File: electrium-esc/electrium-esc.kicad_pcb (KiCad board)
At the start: 2 copper layers, 87.1 x 57.9 mm, 189 parts, among them J1 Debug Connector, J2 USB_MICRO, J3 Conn_01x04_Male, J4 SERVO, J5 Conn_01x04_Male, Q1 IRF3205, Q10 IRF3205, Q11 IRF3205, Q12 IRF3205, Q2 IRF3205, Q3 IRF3205, Q4 IRF3205, Q5 IRF3205, Q6 IRF3205, Q7 IRF3205, Q8 IRF3205, Q9 IRF3205, SW1 SW_SPDT, U1 STM32F407ZGT6, U2 DRV8301DCAR, U3 DRV8301DCAR, U4 SN65HVD232, U5 NRF24L01_Breakout, Y1 25MHz

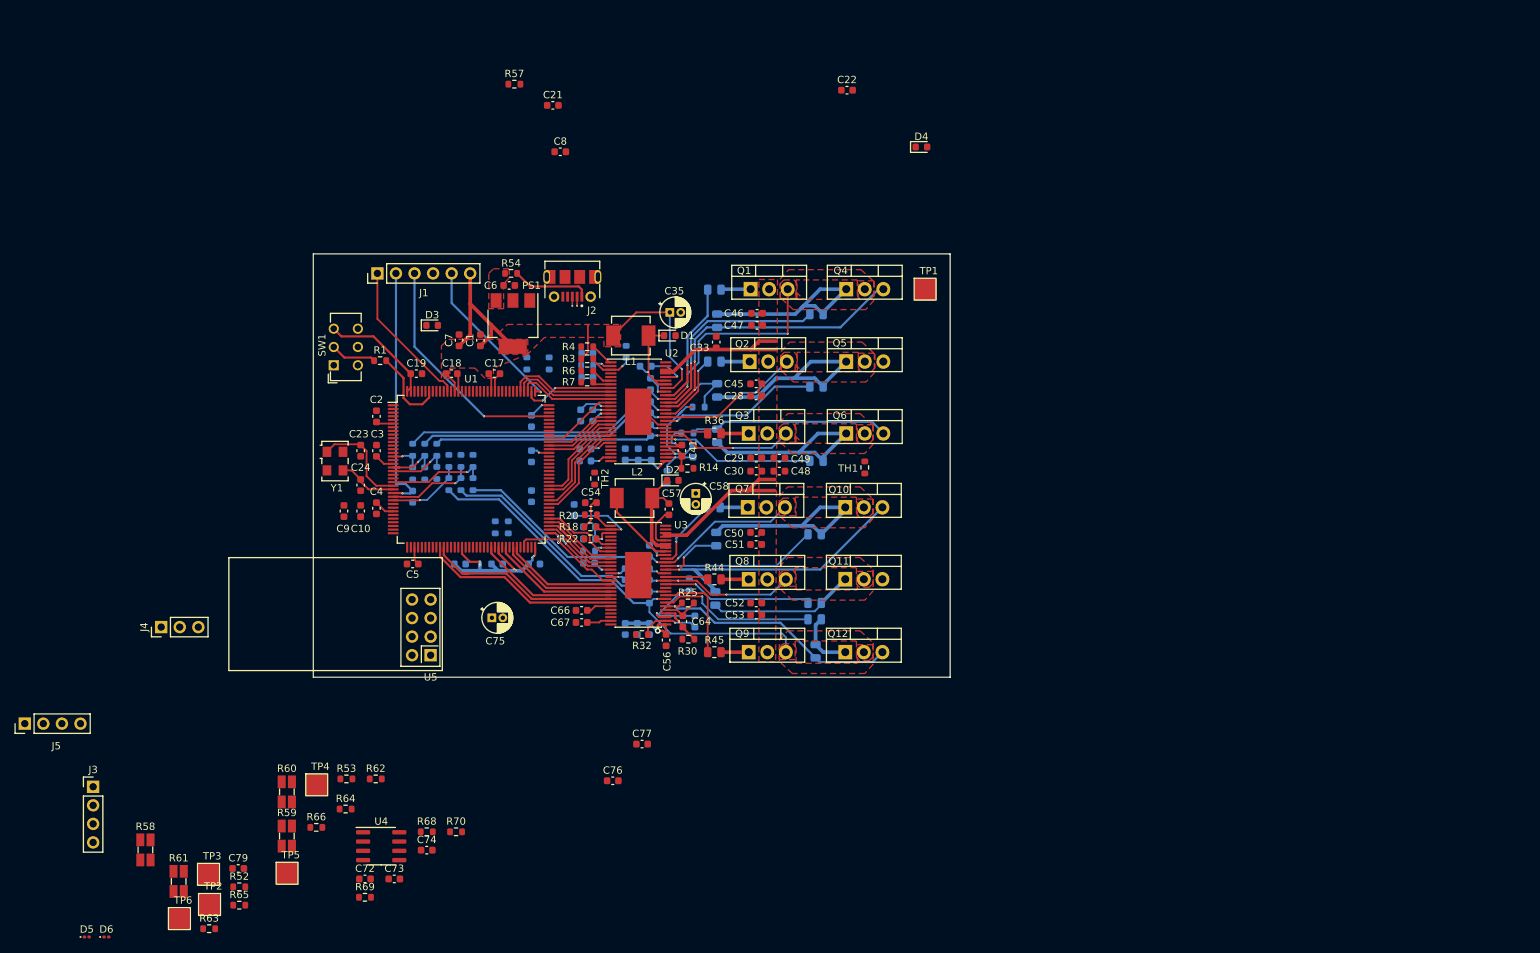
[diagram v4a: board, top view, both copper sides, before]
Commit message: Add power connections
I realize Vias are unrealistic, need to redo.
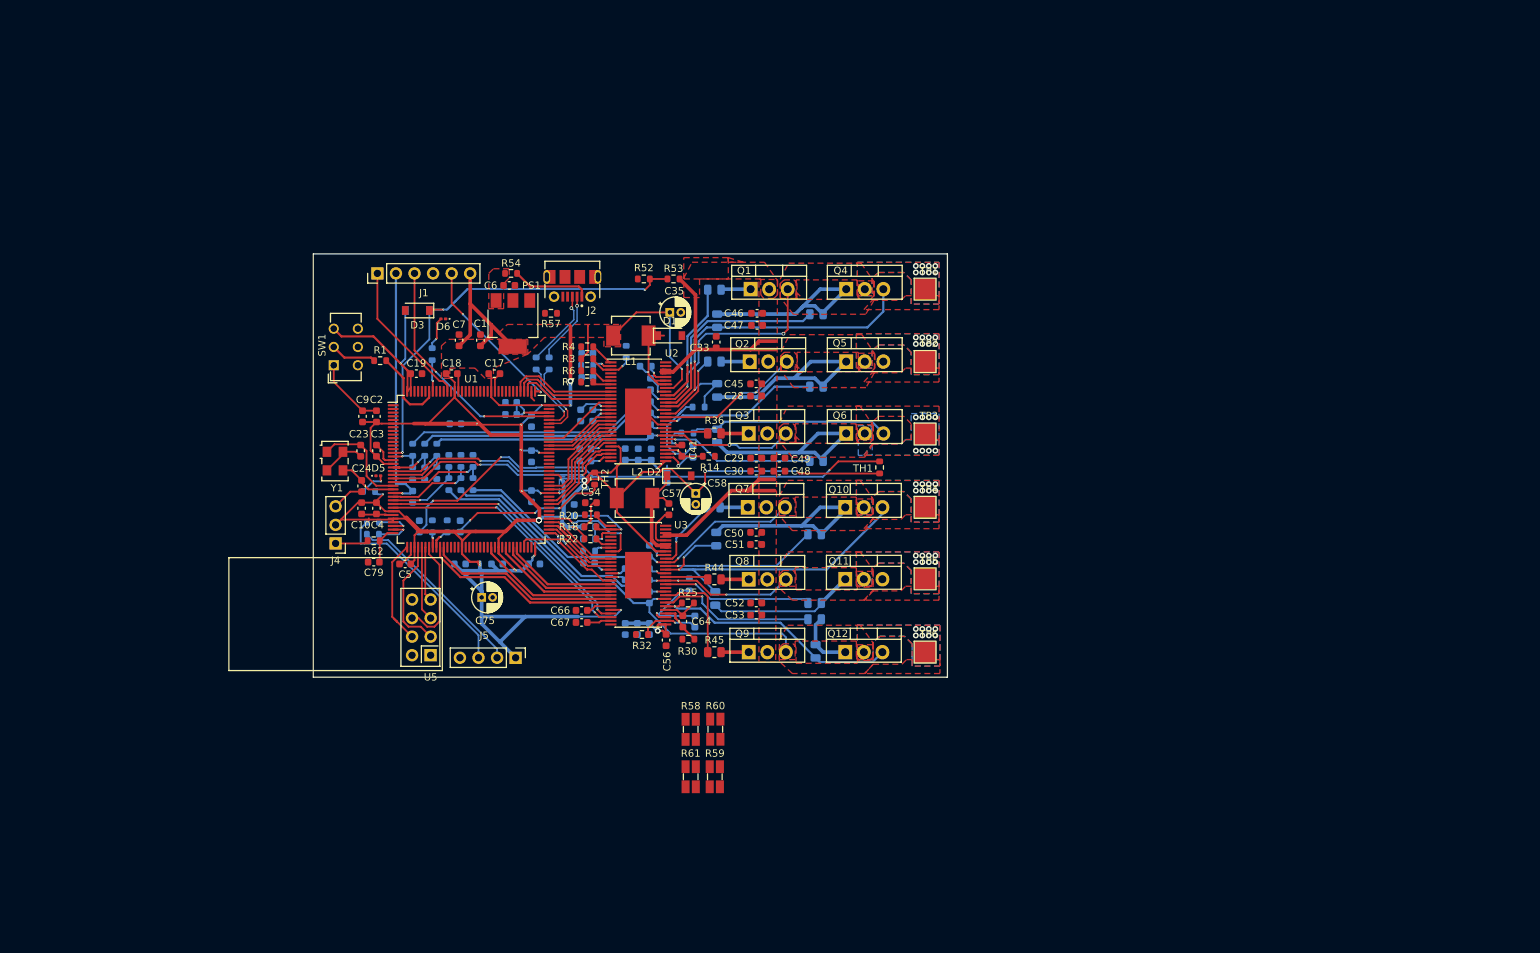
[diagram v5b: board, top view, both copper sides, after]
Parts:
- removed C72, C73, C74: 100n, Capacitor_SMD:C_0603_1608Metric
- removed J3: Conn_01x04_Male, Connector_PinHeader_2.54mm:PinHeader_1x04_P2.54mm_Vertical
- removed R68, R69: 10, Resistor_SMD:R_0603_1608Metric
- removed R70: IN, Resistor_SMD:R_0603_1608Metric
- removed U4: SN65HVD232, Package_SO:SOIC-8_3.9x4.9mm_P1.27mm
- C21, C22, C76, C77, C8, R63, R64, R65, R66: moved to B.Cu
- D1, D2, D3: footprint Diode_SMD:D_0603_1608Metric -> Diode_SMD:D_SOD-123
- D4: footprint Diode_SMD:D_0603_1608Metric -> Diode_SMD:D_SOD-123; moved to B.Cu
- moved TP2 122.9 mm to (186.1, 61.5)
- moved TP3 115.1 mm to (186.1, 71.4)
- moved TP6 108.3 mm to (186.1, 101.2)
- moved R52 99.9 mm to (147.6, 50.2)
- moved D6 96.3 mm to (120.1, 55.6), turned to 180 degrees
- moved TP5 96.1 mm to (186.1, 91.2)
- moved TP4 91.5 mm to (186.1, 81.4)
- moved R53 81.7 mm to (151.6, 50.2)
- moved R58 76.4 mm to (154.0, 111.8)
- moved D5 74.6 mm to (111.3, 77.1)
- moved D4 72.5 mm to (116.6, 54.5)
- moved R61 71.5 mm to (154.0, 118.3)
- moved J5 67.8 mm to (130.0, 102.0), turned to -90 degrees
- moved R66 66.6 mm to (118.6, 60.5), turned to -90 degrees
- moved C22 63.9 mm to (129.4, 68.7), turned to 180 degrees
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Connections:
- J4 pad 2: +5V -> +3.3V
- U1 pad 114: /CAN_RX -> /MCU (STM32F407ZGT6)/CAN_RX
- U1 pad 115: /CAN_TX -> /MCU (STM32F407ZGT6)/CAN_TX
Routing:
- net +3.3V: track 123.0 -> 443.1 mm, vias 10 -> 31
- net /MCU (STM32F407ZGT6)/TEMP_A: track 0.00 -> 74.5 mm, vias 0 -> 4
- net /AN_IN: track 0.00 -> 63.2 mm, vias 0 -> 4
- net /MCU (STM32F407ZGT6)/BR_SO2_B: track 0.00 -> 36.6 mm, vias 0 -> 2
- net /MCU (STM32F407ZGT6)/BR_SO1_B: track 0.00 -> 36.5 mm, vias 0 -> 2
- net /MCU (STM32F407ZGT6)/BR_SO2_A: track 0.00 -> 34.8 mm, vias 0 -> 2
- net /MCU (STM32F407ZGT6)/BR_SO1_A: track 0.00 -> 33.1 mm, vias 0 -> 2
- net GND: track 9.96 -> 41.6 mm
- net Net-(J5-Pad3): track 0.00 -> 28.2 mm
- net /MCU (STM32F407ZGT6)/TEMP_B: track 0.00 -> 26.3 mm, vias 0 -> 4
- net Net-(J5-Pad2): track 0.00 -> 25.5 mm
- net /MCU (STM32F407ZGT6)/NRF_CE: track 0.00 -> 15.8 mm
- net /MCU (STM32F407ZGT6)/NRF_MOSI: track 0.00 -> 15.3 mm
- net /MCU (STM32F407ZGT6)/NRF_CSN: track 0.00 -> 15.0 mm
- net V_SUPPLY: track 59.0 -> 70.9 mm
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- added copper zone on B.Cu, net +3.3V
- added copper zone on B.Cu, net /Motor Driver A (DRV8301)/H1_VS
- added copper zone on B.Cu, net /Motor Driver A (DRV8301)/H2_VS
- added copper zone on B.Cu, net /Motor Driver A (DRV8301)/H3_VS
- added copper zone on B.Cu, net /Motor Driver B (DRV8301)/H1_VS
- added copper zone on B.Cu, net /Motor Driver B (DRV8301)/H2_VS
- added copper zone on B.Cu, net /Motor Driver B (DRV8301)/H3_VS
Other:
- board size 87.1 x 57.9 mm -> 86.7 x 57.9 mm

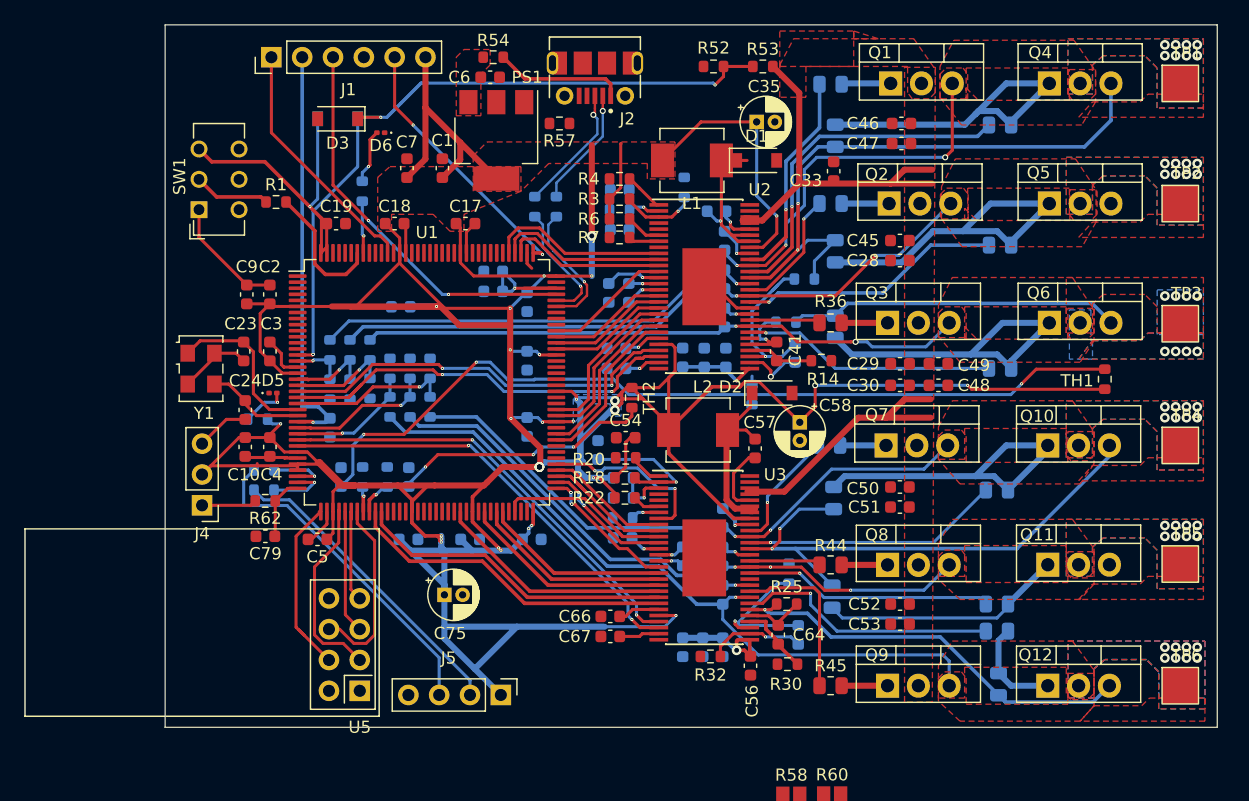
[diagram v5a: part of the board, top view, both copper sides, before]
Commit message: Fix most ERC errors, just some connections now!
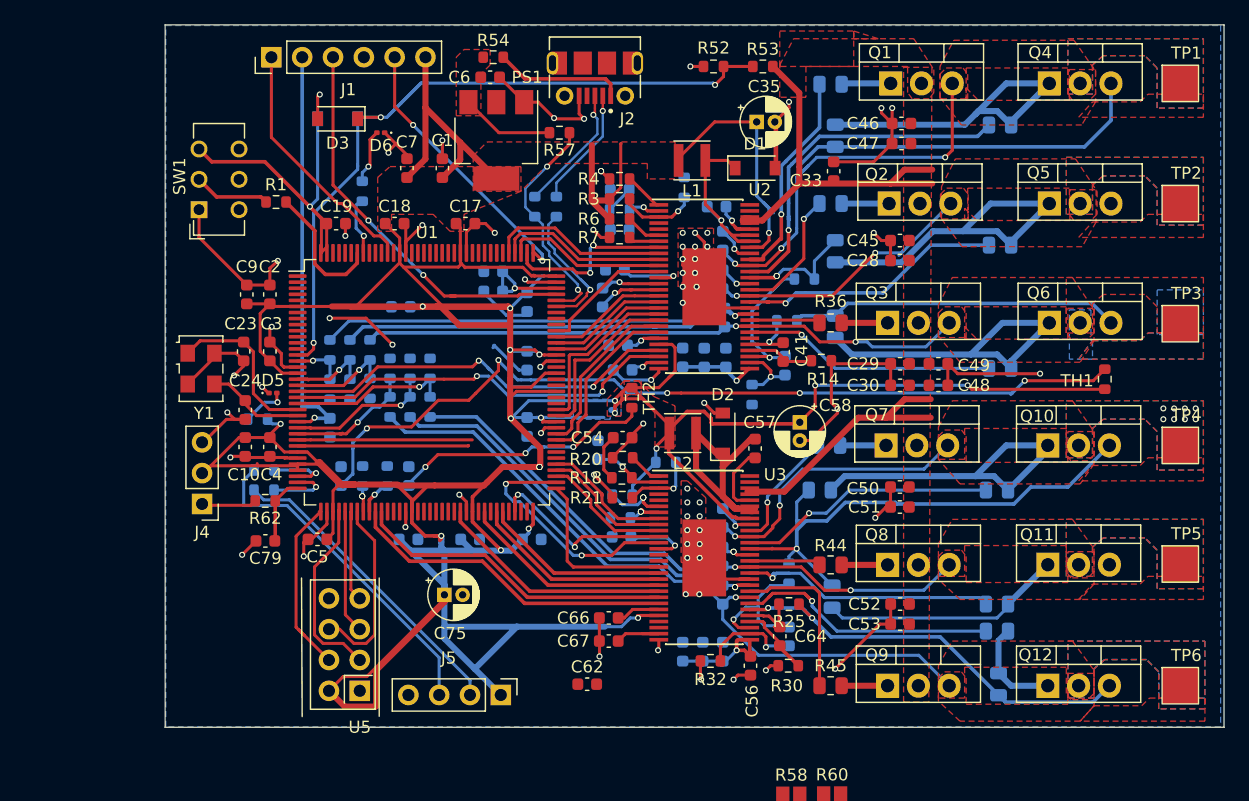
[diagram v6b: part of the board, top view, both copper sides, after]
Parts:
- C62, R21: moved to F.Cu
- L1, L2: footprint Inductor_SMD:L_Vishay_IHLP-2020 -> Inductor_SMD:L_Taiyo-Yuden_NR-30xx
- R22: moved to B.Cu
- moved C62 13.2 mm to (137.2, 101.1), turned to 0 degrees
- moved D2 5.24 mm to (148.3, 80.4), turned to 90 degrees
- moved R19 3.78 mm to (143.6, 82.8)
- moved C39 2.19 mm to (138.4, 69.2)
- moved C37 1.97 mm to (139.4, 66.9), turned to 0 degrees
- moved C42 1.34 mm to (153.5, 74.8)
- moved R49 1.32 mm to (156.3, 85.1), turned to 180 degrees
- moved L2 1.30 mm to (145.0, 80.4)
- moved C65 0.77 mm to (153.8, 97.2)
- moved R57 0.76 mm to (134.9, 55.6)
- moved D1 0.65 mm to (151.0, 58.5)
- moved C41 0.54 mm to (153.3, 73.7)
- moved C44 0.52 mm to (140.1, 75.2)
- moved C67 0.40 mm to (138.9, 97.5)
- moved C34 0.38 mm to (147.8, 61.7)
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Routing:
- net GND: track 41.6 -> 207.7 mm, vias 0 -> 70
- net +3.3V: track 443.1 -> 474.9 mm, vias 31 -> 21
- net /MCU (STM32F407ZGT6)/BR_SO2_B: track 36.6 -> 14.1 mm, vias 2 -> 0
- net /MCU (STM32F407ZGT6)/BR_SO1_B: track 36.5 -> 14.4 mm, vias 2 -> 0
- net /MCU (STM32F407ZGT6)/CS_A: track 1.42 -> 15.6 mm, vias 0 -> 3
- net Net-(C57-Pad2): track 15.7 -> 26.4 mm
- net /MCU (STM32F407ZGT6)/DC_CAL_B: track 10.9 -> 20.3 mm
- net /Motor Driver A (DRV8301)/H1_LOW: track 50.2 -> 40.9 mm
- net /MCU (STM32F407ZGT6)/USB_D+: track 10.2 -> 19.0 mm, vias 1 -> 2
- net +5V: track 0.00 -> 7.72 mm
- net /Motor Driver B (DRV8301)/H1_VS: track 49.9 -> 56.0 mm
- net /Motor Driver B (DRV8301)/COMP: track 10.8 -> 5.86 mm
- net /Motor Driver A (DRV8301)/H1_VS: track 68.0 -> 72.8 mm, vias 11 -> 3
- net /MCU (STM32F407ZGT6)/CS_B: track 14.5 -> 10.7 mm, vias 2 -> 0
- net /Motor Driver B (DRV8301)/GVDD: track 2.58 -> 6.17 mm
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- added copper zone on B.Cu, net GND
- added copper zone on F.Cu, net GND
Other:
- board size 86.7 x 57.9 mm -> 87.3 x 57.9 mm

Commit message: Did a bit more work, almost done!
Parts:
- moved R57 0.25 mm to (134.9, 55.4)
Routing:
- net /Motor Driver A (DRV8301)/H1_LOW: track 40.9 -> 59.0 mm
- net V_SUPPLY: track 70.9 -> 88.5 mm
- net /MCU (STM32F407ZGT6)/TEMP_B: track 27.9 -> 17.4 mm, vias 4 -> 3
- net +3.3V: track 474.9 -> 468.7 mm, vias 21 -> 18
- net Net-(C21-Pad1): track 8.00 -> 10.3 mm
- net /MCU (STM32F407ZGT6)/USB_D+: track 19.0 -> 21.0 mm
- net GND: track 207.7 -> 206.0 mm, vias 70 -> 69
- net /Motor Driver A (DRV8301)/H2_VS: track 55.9 -> 57.1 mm, vias 2 -> 10
- net Net-(Q5-Pad1): track 28.8 -> 27.8 mm
- net /MCU (STM32F407ZGT6)/DC_CAL_B: track 20.3 -> 21.1 mm
- net Net-(C34-Pad2): track 15.4 -> 14.6 mm
- net /Motor Driver B (DRV8301)/H3_VS: vias 1 -> 9
- net /Motor Driver B (DRV8301)/H2_VS: vias 2 -> 10
- net /Motor Driver A (DRV8301)/H3_VS: vias 2 -> 10
- net /Motor Driver A (DRV8301)/H1_VS: vias 3 -> 11
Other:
- board size 87.3 x 57.9 mm -> 90 x 60 mm

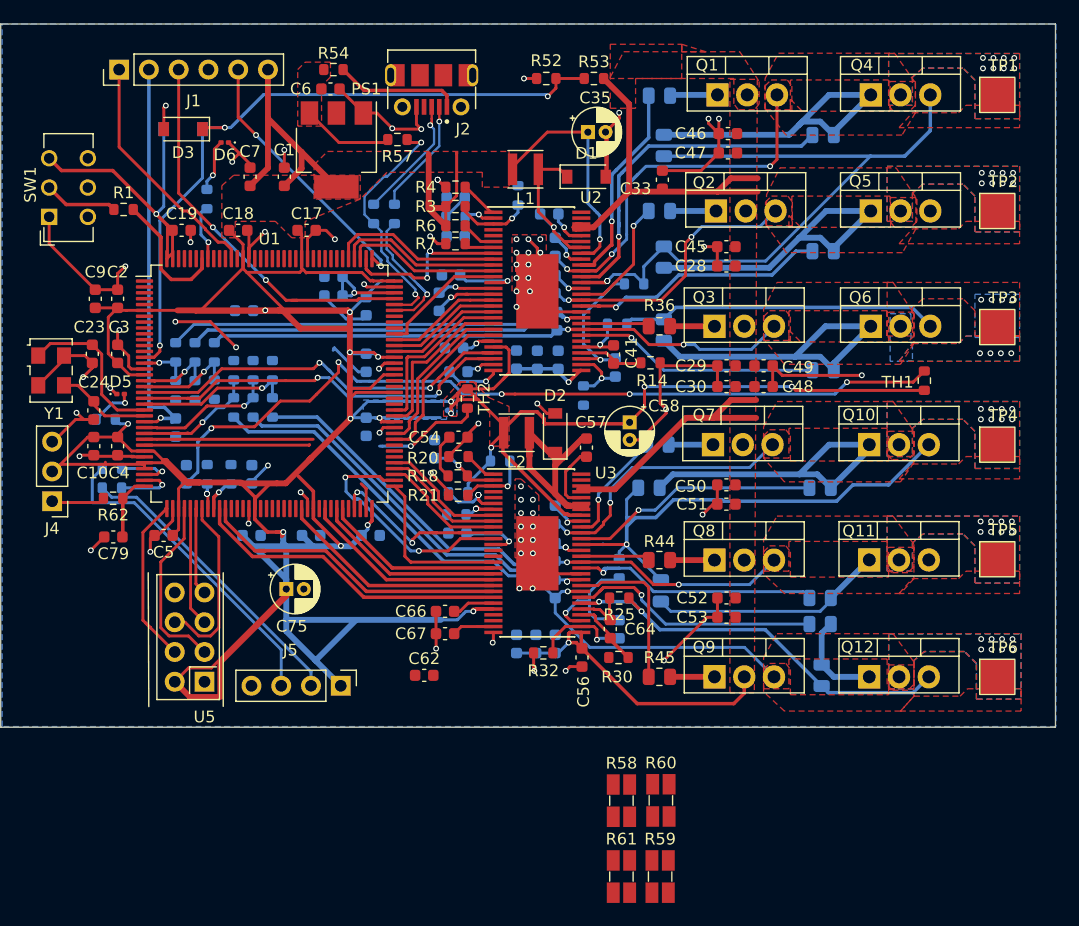
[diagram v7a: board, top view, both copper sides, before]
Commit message: Add Shunt resistors and fixed DRC errors
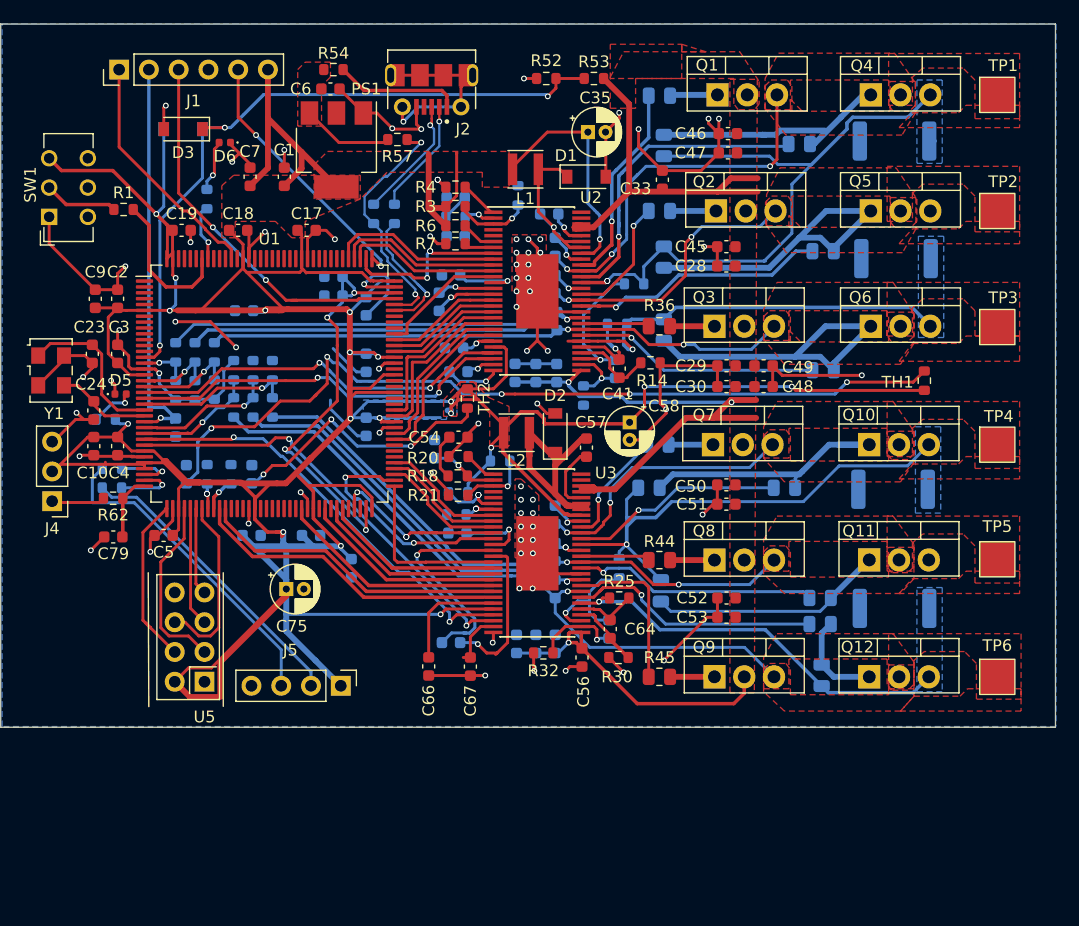
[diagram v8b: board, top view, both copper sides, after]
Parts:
- C62: moved to B.Cu
- D5, D6: footprint Diode_SMD:D_0201_0603Metric -> Diode_SMD:D_0402_1005Metric
- R58, R59, R60, R61: footprint Resistor_SMD:R_Shunt_Ohmite_LVK12 -> Resistor_SMD:R_2512_6332Metric; moved to B.Cu
- moved R59 65.9 mm to (177.3, 55.5), turned to 180 degrees
- moved R58 51.8 mm to (177.4, 65.5), turned to 180 degrees
- moved R61 40.4 mm to (177.2, 85.2), turned to 180 degrees
- moved R60 25.8 mm to (177.3, 95.4), turned to 180 degrees
- moved C66 4.90 mm to (137.5, 100.3), turned to 90 degrees
- moved C62 3.61 mm to (139.4, 98.3), turned to 180 degrees
- moved C67 3.54 mm to (141.1, 100.3), turned to -90 degrees
- moved C13 3.25 mm to (130.9, 91.9), turned to -90 degrees
- moved R46 3.05 mm to (167.9, 85.1)
- moved R37 2.17 mm to (169.2, 55.8)
- moved C41 1.30 mm to (153.8, 74.9)
- moved C26 1.14 mm to (146.7, 75.3)
- moved C27 1.14 mm to (148.5, 75.3)
- moved C25 1.14 mm to (144.9, 75.3)
- moved C65 0.89 mm to (152.9, 97.2)
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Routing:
- net GND: track 206.0 -> 240.6 mm, vias 69 -> 74
- net +3.3V: track 468.7 -> 437.8 mm, vias 18 -> 19
- net Net-(C21-Pad1): track 10.3 -> 36.3 mm, vias 1 -> 4
- net /MCU (STM32F407ZGT6)/BR_SO1_B: track 14.4 -> 38.1 mm, vias 0 -> 2
- net /MCU (STM32F407ZGT6)/BR_SO2_B: track 14.1 -> 37.4 mm, vias 0 -> 2
- net Net-(C62-Pad2): track 0.00 -> 18.5 mm, vias 0 -> 1
- net unconnected-(J2-PadSH1): track 0.00 -> 16.8 mm, vias 0 -> 1
- net V_SUPPLY: track 88.5 -> 103.7 mm, vias 2 -> 3
- net Net-(C62-Pad1): track 0.00 -> 13.5 mm, vias 0 -> 1
- net /MCU (STM32F407ZGT6)/TEMP_B: track 17.4 -> 29.7 mm, vias 3 -> 4
- net /Motor Driver A (DRV8301)/H3_LOW: track 27.2 -> 36.0 mm, vias 0 -> 1
- net Net-(Q4-Pad1): track 27.3 -> 21.0 mm
- net /Motor Driver B (DRV8301)/DVDD: track 3.64 -> 9.67 mm
- net Net-(C41-Pad1): track 5.18 -> 9.63 mm
- net Net-(Q10-Pad1): track 27.3 -> 23.8 mm
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- added copper zone on B.Cu, net /Motor Driver A (DRV8301)/H1_LOW
- added copper zone on B.Cu, net /Motor Driver A (DRV8301)/H3_LOW
- added copper zone on B.Cu, net /Motor Driver B (DRV8301)/H1_LOW
- added copper zone on B.Cu, net /Motor Driver B (DRV8301)/H3_LOW
- removed copper zone on B.Cu, net /Motor Driver A (DRV8301)/H1_VS
- removed copper zone on B.Cu, net /Motor Driver A (DRV8301)/H2_VS
- removed copper zone on B.Cu, net /Motor Driver A (DRV8301)/H3_VS
- removed copper zone on B.Cu, net /Motor Driver B (DRV8301)/H1_VS
- removed copper zone on B.Cu, net /Motor Driver B (DRV8301)/H2_VS
- removed copper zone on B.Cu, net /Motor Driver B (DRV8301)/H3_VS
